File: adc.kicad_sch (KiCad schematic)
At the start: 28 parts, among them IC1 ATM90E26-YU-B, J1 Barrel_Jack_Switch_Pin3Ring, J2 AudioJack3, J4 AudioJack3, Y1 8.192Mhz

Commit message: fix: init symbols references
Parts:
- renumbered C15 to C1, C3 to C10, C17 to C11, C9 to C12, C10 to C13, C1 to C3, C16 to C4, C4 to C5, C5 to C6, C6 to C7, C7 to C8, C8 to C9, IC1 to IC2, J4 to J3, J1 to J4, R3 to R1, R4 to R2, R5 to R3, R6 to R4, R7 to R5

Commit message: fix: assigned FP for ICs
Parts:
- IC2: footprint SOP65P778X199-28N -> ATM90E26-YU-B:SOP65P778X199-28N
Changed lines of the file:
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@@
       (effects (font (size 1.27 1.27)))
     )
-    (property "Footprint" "SOP65P778X199-28N" (at 189.23 173.66 0)
+    (property "Footprint" "ATM90E26-YU-B:SOP65P778X199-28N" (at 189.23 173.66 0)
       (effects (font (size 1.27 1.27)) (justify left top) hide)
     )

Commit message: stagged
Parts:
- removed RN1: 1K, Resistor_SMD:R_Array_Convex_4x1206, symbol Device:R_Pack06_Split
- added RN1: 1k, Resistor_THT:R_Array_SIP12, symbol Device:R_Pack06_SIP_Split
- R1, R2, R3, R4, R5: footprint Resistor_THT:R_Array_SIP4 -> Resistor_THT:R_Axial_DIN0207_L6.3mm_D2.5mm_P7.62mm_Horizontal
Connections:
- net GND: now also RN1.12 (R6.2), RN1.9 (R5.1)
- net at R4.2: now also J3.S, RN1.3 (R2.1); no longer J3.T
- net at C3.1, IC2.10 (I1P): now also RN1.4 (R2.2)
- net at R3.1: now also J3.T, RN1.1 (R1.1); no longer J3.S
- net at C10.1, IC2.15 (VN): now also RN1.11 (R6.1)
- net at C1.1, IC2.7 (I2P): now also RN1.8 (R4.2)
- net at C2.2, IC2.8 (I2N): now also RN1.6 (R3.2)
- net at J2.T: now also R1.1, RN1.5 (R3.1); no longer R2.2
- net at C11.1, IC2.16 (VP), R5.2: now also RN1.10 (R5.2)
- net at J2.S: now also R2.2, RN1.7 (R4.1); no longer R1.1
- net at C4.2, IC2.11 (I1N): now also RN1.2 (R1.2)
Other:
- moved on the sheet: R1, R2, R3, R4

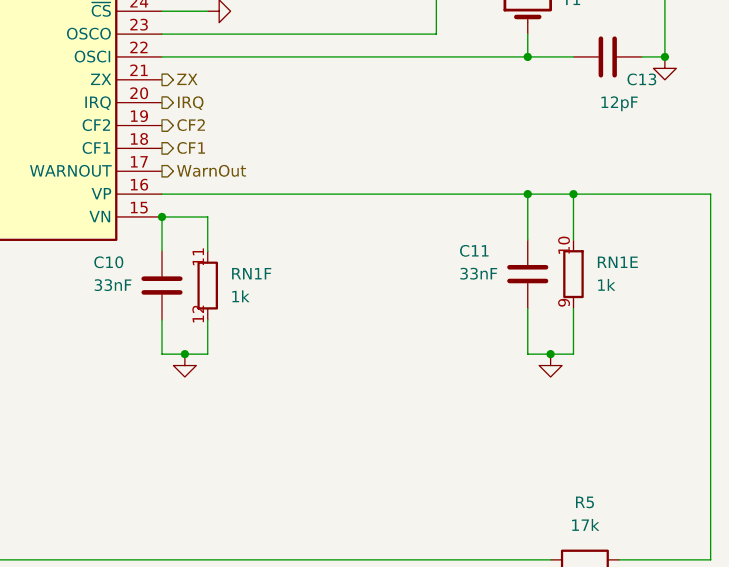
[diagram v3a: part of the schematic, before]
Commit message: refactor: split 6 resistors network of low band filters in 2 + 4 networks
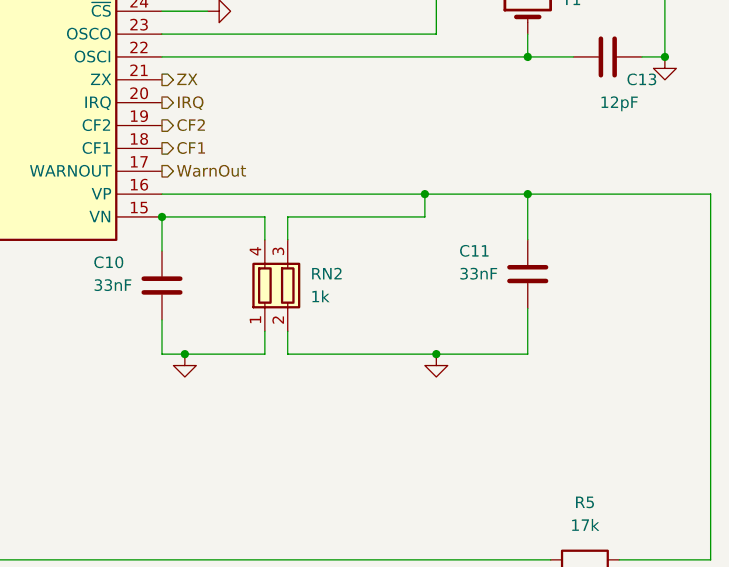
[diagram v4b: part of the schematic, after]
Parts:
- removed unit 5 of RN1
- removed unit 6 of RN1
- added RN2: 1k, Package_DIP:DIP-4_W7.62mm, symbol Device:R_Pack02
- RN1: footprint Resistor_THT:R_Array_SIP12 -> Resistor_THT:R_Array_SIP8
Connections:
- net GND: now also RN2.1 (R1.1), RN2.2 (R2.1)
- net at C10.1, IC2.15 (VN): now also RN2.4 (R1.2)
- net at C11.1, IC2.16 (VP), R5.2: now also RN2.3 (R2.2)

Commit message: FP: first FP update
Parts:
- C8: footprint Capacitor_SMD:C_0805_2012Metric_Pad1.18x1.45mm_HandSolder -> Capacitor_SMD:C_0603_1608Metric
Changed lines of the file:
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@@
       (effects (font (size 1.27 1.27)) (justify left))
     )
-    (property "Footprint" "Capacitor_SMD:C_0805_2012Metric_Pad1.18x1.45mm_HandSolder" (at 135.5852 120.65 0)
+    (property "Footprint" "Capacitor_SMD:C_0603_1608Metric" (at 135.5852 120.65 0)
       (effects (font (size 1.27 1.27)) hide)
     )
-    (property "Datasheet" "~" (at 134.62 116.84 0)
+    (property "Datasheet" "2 dispo en x7r 547-113-17" (at 134.62 116.84 0)
       (effects (font (size 1.27 1.27)) hide)
     )

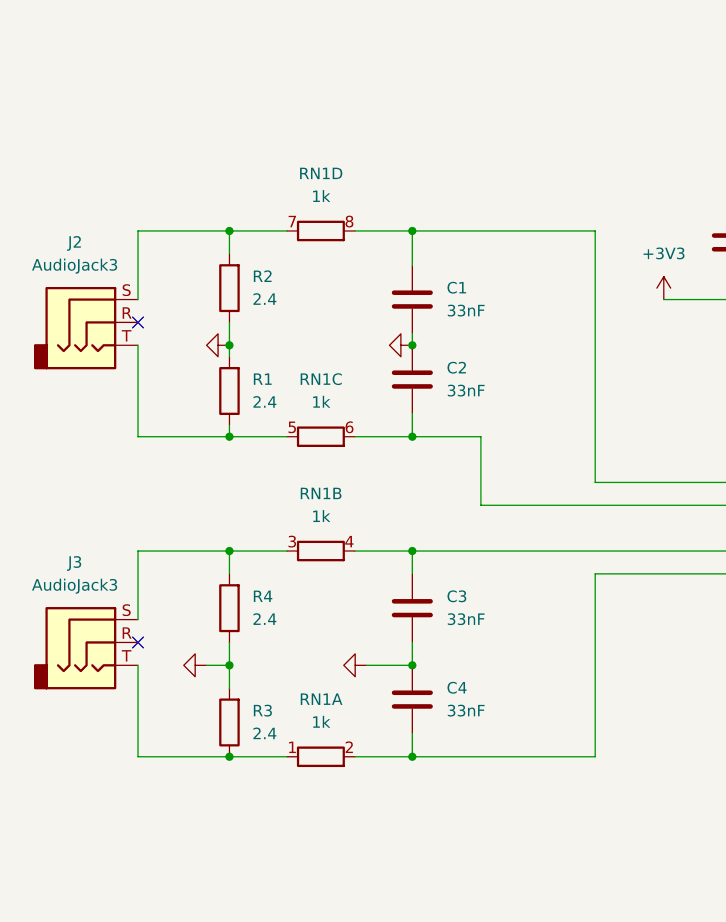
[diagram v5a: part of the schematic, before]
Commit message: FP: update 1k resistor array to smd FP
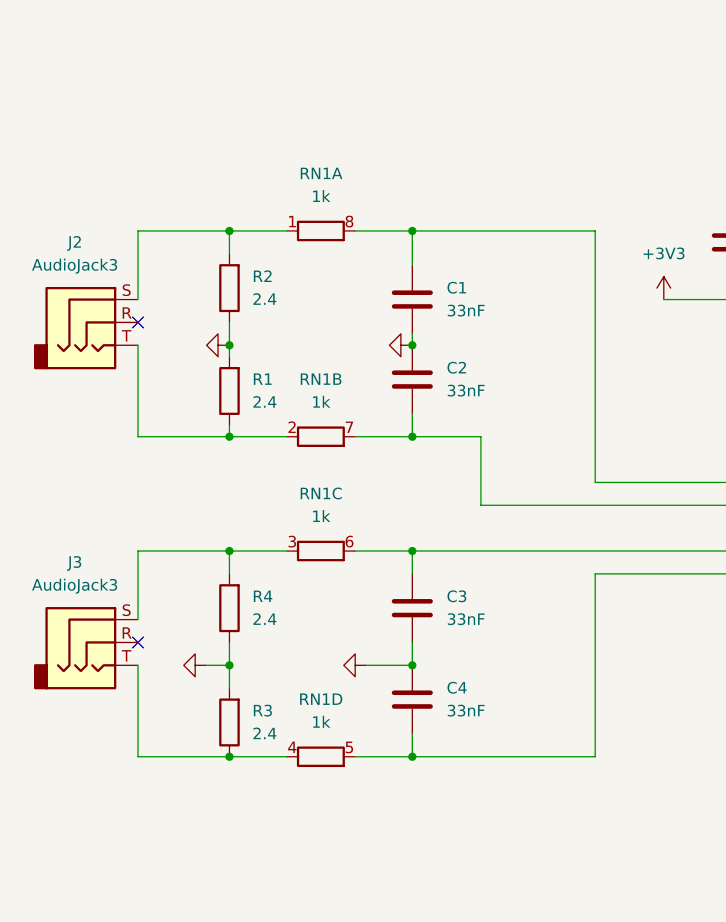
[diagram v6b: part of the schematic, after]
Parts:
- removed RN1: 1k, Resistor_THT:R_Array_SIP8, symbol Device:R_Pack06_SIP_Split
- added RN1: 1k, Resistor_SMD:R_Array_Convex_4x0603, symbol Device:R_Pack04_Split
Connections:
- net at J3.S, R4.2: now also RN1.3 (R3.1)
- net at C1.1, IC2.7 (I2P): now also RN1.8 (R1.2)
- net at C3.1, IC2.10 (I1P): now also RN1.6 (R3.2)
- net at J3.T, R3.1: now also RN1.4 (R4.1)
- net at C4.2, IC2.11 (I1N): now also RN1.5 (R4.2)
- net at C2.2, IC2.8 (I2N): now also RN1.7 (R2.2)
- net at J2.T, R1.1: now also RN1.2 (R2.1)
- net at J2.S, R2.2: now also RN1.1 (R1.1)
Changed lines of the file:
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@@
+    )
+  )
+  (symbol (lib_id "Device:R_Pack04_Split") (at 50.8 66.04 270) (unit 1)
+    (in_bom yes) (on_board yes) (dnp no) (fields_autoplaced)
+    (property "Reference" "RN1" (at 50.8 59.69 90)
+      (effects (font (size 1.27 1.27)))
+    )
+    (property "Value" "1k" (at 50.8 62.23 90)
+      (effects (font (size 1.27 1.27)))
+    )
+    (property "Footprint" "Resistor_SMD:R_Array_Convex_4x0603" (at 50.8 64.008 90)
+      (effects (font (size 1.27 1.27)) hide)
+    )
+    (property "Datasheet" "~" (at 50.8 66.04 0)
+      (effects (font (size 1.27 1.27)) hide)
+    )
+    (pin "4")
+    (pin "2")
+    (pin "8")
+    (pin "1")
+    (pin "6")
+    (pin "3")
+    (pin "7")
+    (pin "5")
+    (instances
+      (project "pv_router"
+        (path "/08ef31dc-81c2-4bcd-8336-e62c344e451e/c04c621c-1838-44d9-9dae-69912433c007"
+          (reference "RN1") (unit 1)
+        )
+      )
     )
   )
@@
     )
   )
+  (symbol (lib_id "Device:R_Pack04_Split") (at 50.8 101.6 270) (unit 3)
+    (in_bom yes) (on_board yes) (dnp no) (fields_autoplaced)
+    (property "Reference" "RN1" (at 50.8 95.25 90)
+      (effects (font (size 1.27 1.27)))
+    )
+    (property "Value" "1k" (at 50.8 97.79 90)
+      (effects (font (size 1.27 1.27)))
+    )
+    (property "Footprint" "Resistor_SMD:R_Array_Convex_4x0603" (at 50.8 99.568 90)
+      (effects (font (size 1.27 1.27)) hide)
+    )
+    (property "Datasheet" "~" (at 50.8 101.6 0)
+      (effects (font (size 1.27 1.27)) hide)
+    )
+    (pin "4")
+    (pin "2")
+    (pin "8")
+    (pin "1")
+    (pin "6")
+    (pin "3")
+    (pin "7")
+    (pin "5")
+    (instances
+      (project "pv_router"
+        (path "/08ef31dc-81c2-4bcd-8336-e62c344e451e/c04c621c-1838-44d9-9dae-69912433c007"
+          (reference "RN1") (unit 3)
+        )
+      )
+    )
+  )
+  (symbol (lib_id "Device:R_Pack04_Split") (at 50.8 88.9 270) (unit 2)
+    (in_bom yes) (on_board yes) (dnp no) (fields_autoplaced)
+    (property "Reference" "RN1" (at 50.8 82.55 90)
+      (effects (font (size 1.27 1.27)))
+    )
+    (property "Value" "1k" (at 50.8 85.09 90)
+      (effects (font (size 1.27 1.27)))
+    )
+    (property "Footprint" "Resistor_SMD:R_Array_Convex_4x0603" (at 50.8 86.868 90)
+      (effects (font (size 1.27 1.27)) hide)
+    )
+    (property "Datasheet" "~" (at 50.8 88.9 0)
+      (effects (font (size 1.27 1.27)) hide)
+    )
+    (pin "4")
+    (pin "2")
+    (pin "8")
+    (pin "1")
+    (pin "6")
+    (pin "3")
+    (pin "7")
+    (pin "5")
+    (instances
+      (project "pv_router"
+        (path "/08ef31dc-81c2-4bcd-8336-e62c344e451e/c04c621c-1838-44d9-9dae-69912433c007"
+          (reference "RN1") (unit 2)
+        )
+      )
+    )
+  )
   (symbol (lib_id "Jumper:Jumper_2_Bridged") (at 177.8 45.72 270) (unit 1)
     (in_bom yes) (on_board yes) (dnp no) (fields_autoplaced)
@@
         (path "/08ef31dc-81c2-4bcd-8336-e62c344e451e/c04c621c-1838-44d9-9dae-69912433c007"
           (reference "JP3") (unit 1)
-        )
-      )
-    )
-  )
-  (symbol (lib_id "Device:R_Pack06_SIP_Split") (at 50.8 124.46 270) (unit 1)
-    (in_bom yes) (on_board yes) (dnp no) (fields_autoplaced)
-    (property "Reference" "RN1" (at 50.8 118.11 90)
-      (effects (font (size 1.27 1.27)))
-    )
-    (property "Value" "1k" (at 50.8 120.65 90)
-      (effects (font (size 1.27 1.27)))
-    )
-    (property "Footprint" "Resistor_THT:R_Array_SIP8" (at 50.8 122.428 90)
-      (effects (font (size 1.27 1.27)) hide)
-    )
-    (property "Datasheet" "http://www.vishay.com/docs/31509/csc.pdf" (at 50.8 124.46 0)
-      (effects (font (size 1.27 1.27)) hide)
-    )
-    (pin "11")
-    (pin "6")
-    (pin "7")
-    (pin "2")
-    (pin "9")
-    (pin "5")
-    (pin "4")
-    (pin "3")
-    (pin "1")
-    (pin "12")
-    (pin "8")
-    (pin "10")
-    (instances
-      (project "pv_router"
-        (path "/08ef31dc-81c2-4bcd-8336-e62c344e451e/c04c621c-1838-44d9-9dae-69912433c007"
-          (reference "RN1") (unit 1)
         )
       )
@@
     )
   )
-  (symbol (lib_id "Device:R_Pack06_SIP_Split") (at 50.8 88.9 270) (unit 3)
-    (in_bom yes) (on_board yes) (dnp no) (fields_autoplaced)
-    (property "Reference" "RN1" (at 50.8 82.55 90)
-      (effects (font (size 1.27 1.27)))
-    )
-    (property "Value" "1k" (at 50.8 85.09 90)
-      (effects (font (size 1.27 1.27)))
-    )
-    (property "Footprint" "Resistor_THT:R_Array_SIP8" (at 50.8 86.868 90)
-      (effects (font (size 1.27 1.27)) hide)
-    )
-    (property "Datasheet" "http://www.vishay.com/docs/31509/csc.pdf" (at 50.8 88.9 0)
-      (effects (font (size 1.27 1.27)) hide)
-    )
-    (pin "11")
-    (pin "6")
-    (pin "7")
-    (pin "2")
-    (pin "9")
-    (pin "5")
-    (pin "4")
-    (pin "3")
-    (pin "1")
-    (pin "12")
-    (pin "8")
-    (pin "10")
-    (instances
-      (project "pv_router"
-        (path "/08ef31dc-81c2-4bcd-8336-e62c344e451e/c04c621c-1838-44d9-9dae-69912433c007"
-          (reference "RN1") (unit 3)
-        )
-      )
-    )
-  )
   (symbol (lib_id "Connector_Audio:AudioJack3") (at 25.4 111.76 0) (unit 1)
     (in_bom yes) (on_board yes) (dnp no) (fields_autoplaced)
@@
     )
   )
-  (symbol (lib_id "Device:R_Pack06_SIP_Split") (at 50.8 101.6 270) (unit 2)
-    (in_bom yes) (on_board yes) (dnp no) (fields_autoplaced)
-    (property "Reference" "RN1" (at 50.8 95.25 90)
-      (effects (font (size 1.27 1.27)))
-    )
-    (property "Value" "1k" (at 50.8 97.79 90)
-      (effects (font (size 1.27 1.27)))
-    )
-    (property "Footprint" "Resistor_THT:R_Array_SIP8" (at 50.8 99.568 90)
-      (effects (font (size 1.27 1.27)) hide)
-    )
-    (property "Datasheet" "http://www.vishay.com/docs/31509/csc.pdf" (at 50.8 101.6 0)
-      (effects (font (size 1.27 1.27)) hide)
-    )
-    (pin "11")
+  (symbol (lib_id "Device:R_Pack04_Split") (at 50.8 124.46 270) (unit 4)
+    (in_bom yes) (on_board yes) (dnp no) (fields_autoplaced)
+    (property "Reference" "RN1" (at 50.8 118.11 90)
+      (effects (font (size 1.27 1.27)))
+    )
+    (property "Value" "1k" (at 50.8 120.65 90)
+      (effects (font (size 1.27 1.27)))
+    )
+    (property "Footprint" "Resistor_SMD:R_Array_Convex_4x0603" (at 50.8 122.428 90)
+      (effects (font (size 1.27 1.27)) hide)
+    )
+    (property "Datasheet" "~" (at 50.8 124.46 0)
+      (effects (font (size 1.27 1.27)) hide)
+    )
+    (pin "4")
+    (pin "2")
+    (pin "8")
+    (pin "1")
     (pin "6")
+    (pin "3")
     (pin "7")
-    (pin "2")
-    (pin "9")
     (pin "5")
-    (pin "4")
-    (pin "3")
-    (pin "1")
-    (pin "12")
-    (pin "8")
-    (pin "10")
-    (instances
-      (project "pv_router"
-        (path "/08ef31dc-81c2-4bcd-8336-e62c344e451e/c04c621c-1838-44d9-9dae-69912433c007"
-          (reference "RN1") (unit 2)
+    (instances
+      (project "pv_router"
+        (path "/08ef31dc-81c2-4bcd-8336-e62c344e451e/c04c621c-1838-44d9-9dae-69912433c007"
+          (reference "RN1") (unit 4)
         )
       )
@@
         )
       )
-    )
-  )
-  (symbol (lib_id "Device:R_Pack06_SIP_Split") (at 50.8 66.04 270) (unit 4)
-    (in_bom yes) (on_board yes) (dnp no) (fields_autoplaced)
-    (property "Reference" "RN1" (at 50.8 59.69 90)
-      (effects (font (size 1.27 1.27)))
-    )
-    (property "Value" "1k" (at 50.8 62.23 90)
-      (effects (font (size 1.27 1.27)))
-    )
-    (property "Footprint" "Resistor_THT:R_Array_SIP8" (at 50.8 64.008 90)
-      (effects (font (size 1.27 1.27)) hide)
-    )
-    (property "Datasheet" "http://www.vishay.com/docs/31509/csc.pdf" (at 50.8 66.04 0)
-      (effects (font (size 1.27 1.27)) hide)
-    )
-    (pin "11")
-    (pin "6")
-    (pin "7")
-    (pin "2")
-    (pin "9")
-    (pin "5")
-    (pin "4")
-    (pin "3")
-    (pin "1")
-    (pin "12")
-    (pin "8")
-    (pin "10")
-    (instances
-      (project "pv_router"
-        (path "/08ef31dc-81c2-4bcd-8336-e62c344e451e/c04c621c-1838-44d9-9dae-69912433c007"
-          (reference "RN1") (unit 4)
-        )
-      )

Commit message: fix: update FP
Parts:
- Y1: footprint Crystal:Crystal_SMD_FOX_FE-2Pin_7.5x5.0mm_HandSoldering -> Crystal:Crystal_HC18-U_Vertical
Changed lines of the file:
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@@
       (effects (font (size 1.27 1.27)) hide)
     )
-    (property "Datasheet" "~" (at 193.04 119.38 0)
+    (property "Datasheet" "ok : 6" (at 193.04 119.38 0)
       (effects (font (size 1.27 1.27)) hide)
     )
@@
       (effects (font (size 1.27 1.27)) hide)
     )
-    (property "Datasheet" "~" (at 60.96 73.66 0)
+    (property "Datasheet" "ok : 6" (at 60.96 73.66 0)
       (effects (font (size 1.27 1.27)) hide)
     )
@@
       (effects (font (size 1.27 1.27)) hide)
     )
-    (property "Datasheet" "~" (at 242.57 81.28 0)
+    (property "Datasheet" "2 ok" (at 242.57 81.28 0)
       (effects (font (size 1.27 1.27)) hide)
     )
@@
       (effects (font (size 1.27 1.27)) hide)
     )
-    (property "Datasheet" "~" (at 60.96 107.95 0)
+    (property "Datasheet" "ok : 6" (at 60.96 107.95 0)
       (effects (font (size 1.27 1.27)) hide)
     )
@@
       (effects (font (size 1.27 1.27)) hide)
     )
-    (property "Datasheet" "~" (at 50.8 66.04 0)
+    (property "Datasheet" "2 dispo" (at 50.8 66.04 0)
       (effects (font (size 1.27 1.27)) hide)
     )
@@
       (effects (font (size 1.27 1.27)) hide)
     )
-    (property "Datasheet" "~" (at 50.8 101.6 0)
+    (property "Datasheet" "2 dispo" (at 50.8 101.6 0)
       (effects (font (size 1.27 1.27)) hide)
     )
@@
       (effects (font (size 1.27 1.27)) hide)
     )
-    (property "Datasheet" "~" (at 50.8 88.9 0)
+    (property "Datasheet" "2 dispo" (at 50.8 88.9 0)
       (effects (font (size 1.27 1.27)) hide)
     )
@@
       (effects (font (size 1.27 1.27)) hide)
     )
-    (property "Datasheet" "~" (at 233.68 118.11 0)
+    (property "Datasheet" "ok : 6" (at 233.68 118.11 0)
       (effects (font (size 1.27 1.27)) hide)
     )
@@
       (effects (font (size 1.27 1.27)) hide)
     )
-    (property "Datasheet" "~" (at 60.96 118.11 0)
+    (property "Datasheet" "ok : 6" (at 60.96 118.11 0)
       (effects (font (size 1.27 1.27)) hide)
     )
@@
       (effects (font (size 1.27 1.27)) hide)
     )
-    (property "Datasheet" "~" (at 50.8 124.46 0)
+    (property "Datasheet" "2 dispo" (at 50.8 124.46 0)
       (effects (font (size 1.27 1.27)) hide)
     )
@@
       (effects (font (size 1.27 1.27)) hide)
     )
-    (property "Datasheet" "~" (at 242.57 93.98 0)
+    (property "Datasheet" "2 ok" (at 242.57 93.98 0)
       (effects (font (size 1.27 1.27)) hide)
     )
@@
       (effects (font (size 1.27 1.27)) hide)
     )
-    (property "Datasheet" "~" (at 60.96 82.55 0)
+    (property "Datasheet" "ok : 6" (at 60.96 82.55 0)
       (effects (font (size 1.27 1.27)) hide)
     )
@@
       (effects (font (size 1.27 1.27)) hide)
     )
-    (property "Datasheet" "~" (at 207.01 119.38 0)
+    (property "Datasheet" "ok" (at 207.01 119.38 0)
       (effects (font (size 1.27 1.27)) hide)
     )
@@
       (effects (font (size 1.27 1.27)) (justify right) hide)
     )
-    (property "Footprint" "Crystal:Crystal_SMD_FOX_FE-2Pin_7.5x5.0mm_HandSoldering" (at 233.68 87.63 0)
-      (effects (font (size 1.27 1.27)) hide)
-    )
-    (property "Datasheet" "~" (at 233.68 87.63 0)
-      (effects (font (size 1.27 1.27)) hide)
-    )
+    (property "Footprint" "Crystal:Crystal_HC18-U_Vertical" (at 233.68 87.63 0)
+      (effects (font (size 1.27 1.27)) hide)
+    )
+    (property "Datasheet" "1 ok" (at 233.68 87.63 0)
+      (effects (font (size 1.27 1.27)) hide)
+    )
